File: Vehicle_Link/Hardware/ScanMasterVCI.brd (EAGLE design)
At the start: 53 x 39.4 mm, 97 parts, among them IC1 XMEGA32A4U, IC2 TL331, Q1 MMBT4403, Q10 ZXMP6A17G, Q2 MMBT3904, Q3 MMBT3904, Q4 MMBT4403, Q7 MMBT3904, Q8 MMBT4403, Q9 MMPQ3904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

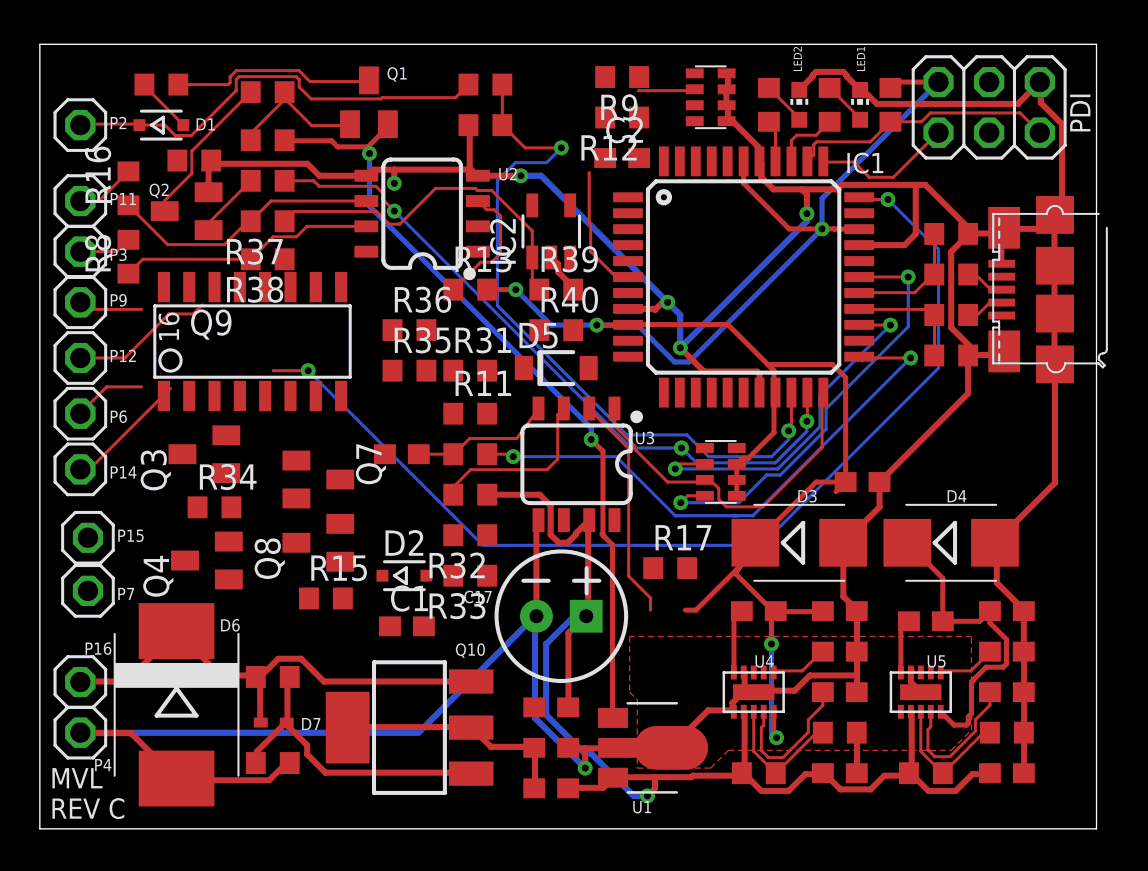
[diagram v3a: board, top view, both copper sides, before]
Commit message: CCD RX circuit tested. Don't have the firmware in a state to test the TX but I want to move forward with new boards for testing. I've finished re-laying out the board. Made a minor change to J1850, switched to a comparator for the RX.
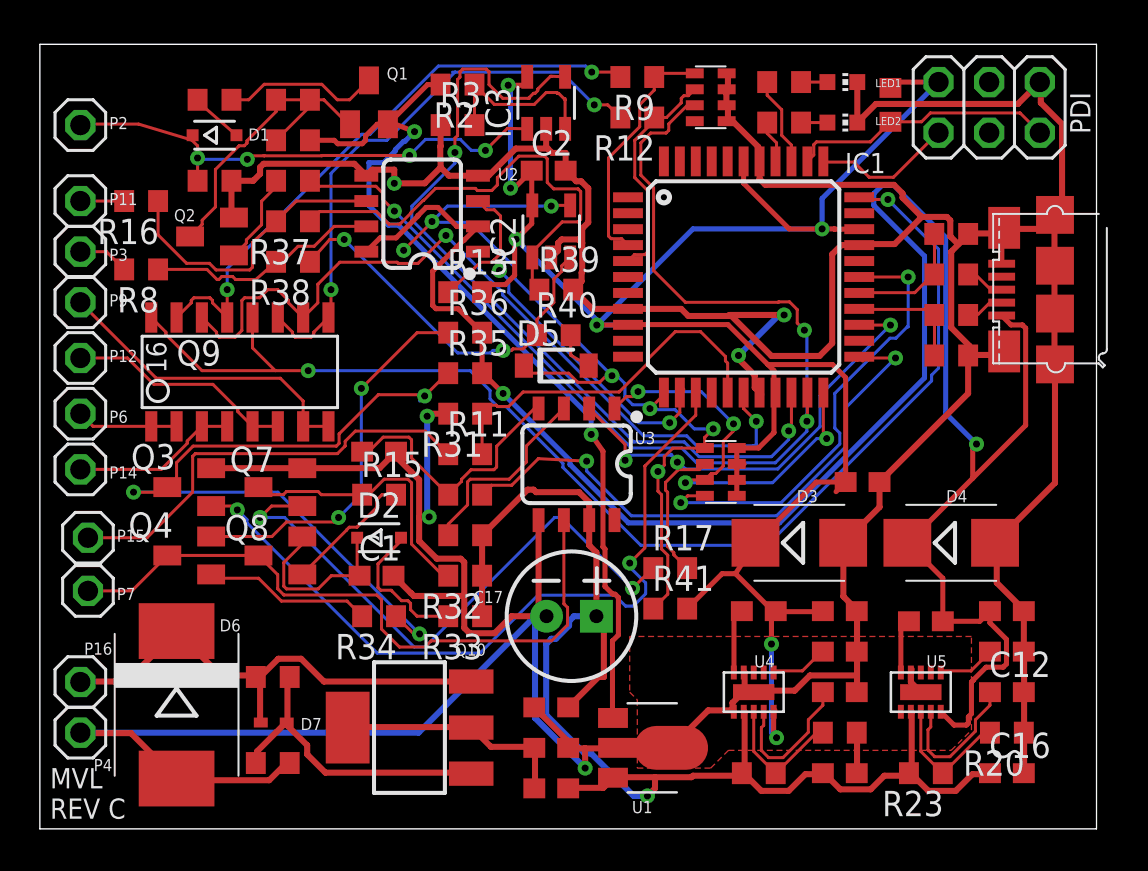
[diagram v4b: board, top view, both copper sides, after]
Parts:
- added IC3: TL331, linear:DBV-R-PDSO-G5
- added R41: 10k, adafruit:R0603
- R2: value 7.5k -> 1k
- R3: value 5k -> 1k
- moved R34 9.90 mm to (17.0, 10.7), turned to 180 degrees
- moved R15 5.85 mm to (17.0, 16.8)
- moved C2 3.74 mm to (25.5, 33.0)
- moved C1 2.96 mm to (16.9, 12.7)
- moved R35 2.80 mm to (21.3, 22.9)
- moved R36 2.80 mm to (21.3, 24.9)
- moved R1 2.77 mm to (8.76, 36.6)
- moved D1 2.71 mm to (8.76, 34.8)
- moved R24 2.56 mm to (37.3, 37.5), turned to 180 degrees
- moved LED2 2.33 mm to (40.3, 35.4), turned to 270 degrees
- moved D2 2.29 mm to (17.0, 14.6)
- moved R31 2.17 mm to (21.3, 20.8), turned to 180 degrees
- moved R10 2.05 mm to (21.3, 16.8)
- moved R11 2.05 mm to (21.3, 18.8)
- moved R14 2.05 mm to (21.3, 14.7)
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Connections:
- removed net SCI-A-ENGINE-EN: IC1.4
- removed net SCI-A-TRANS-EN: IC1.6
- removed net SCI-B-ENGINE-EN: IC1.5
- removed net SCI-B-TRANS-EN: IC1.7
- new net N$37: IC3.3, R2.1, R3.2
- net +3V3: now also IC3.5, R41.2
- net +8V: now also R2.2
- net CCD-RX: now also R41.1
- net GND: now also IC3.2
- net J1850VPW-RX: now also IC3.4; no longer R2.1, R3.2
- net J1962-2: now also IC3.1; no longer R2.2
- net SCI-A-EN: now also IC1.4
- net SCI-B-EN: now also IC1.5
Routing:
- net +5V: track 16.2 -> 104.2 mm, vias 0 -> 2
- net GND: track 237.3 -> 285.0 mm
- net CCD-RX: track 0.09 -> 46.7 mm, vias 0 -> 7
- net SCI-TRANS-TX: track 0.00 -> 40.5 mm, vias 0 -> 2
- net SCI-A-RX-EN: track 0.00 -> 38.4 mm, vias 0 -> 2
- net N$23: track 0.00 -> 38.3 mm, vias 0 -> 3
- net J1962-7: track 0.00 -> 33.8 mm
- net N$1: track 0.00 -> 30.1 mm, vias 0 -> 2
- net N$13: track 0.00 -> 29.4 mm, vias 0 -> 2
- net N$5: track 0.00 -> 28.5 mm, vias 0 -> 2
- net J1850VPW-TX: track 34.9 -> 57.8 mm
- net J1962-15: track 0.00 -> 22.0 mm
- net N$31: track 0.00 -> 19.3 mm, vias 0 -> 2
- net N$35: track 0.00 -> 19.2 mm, vias 0 -> 2
- net SCI-TRANS-RX: track 0.00 -> 18.5 mm
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
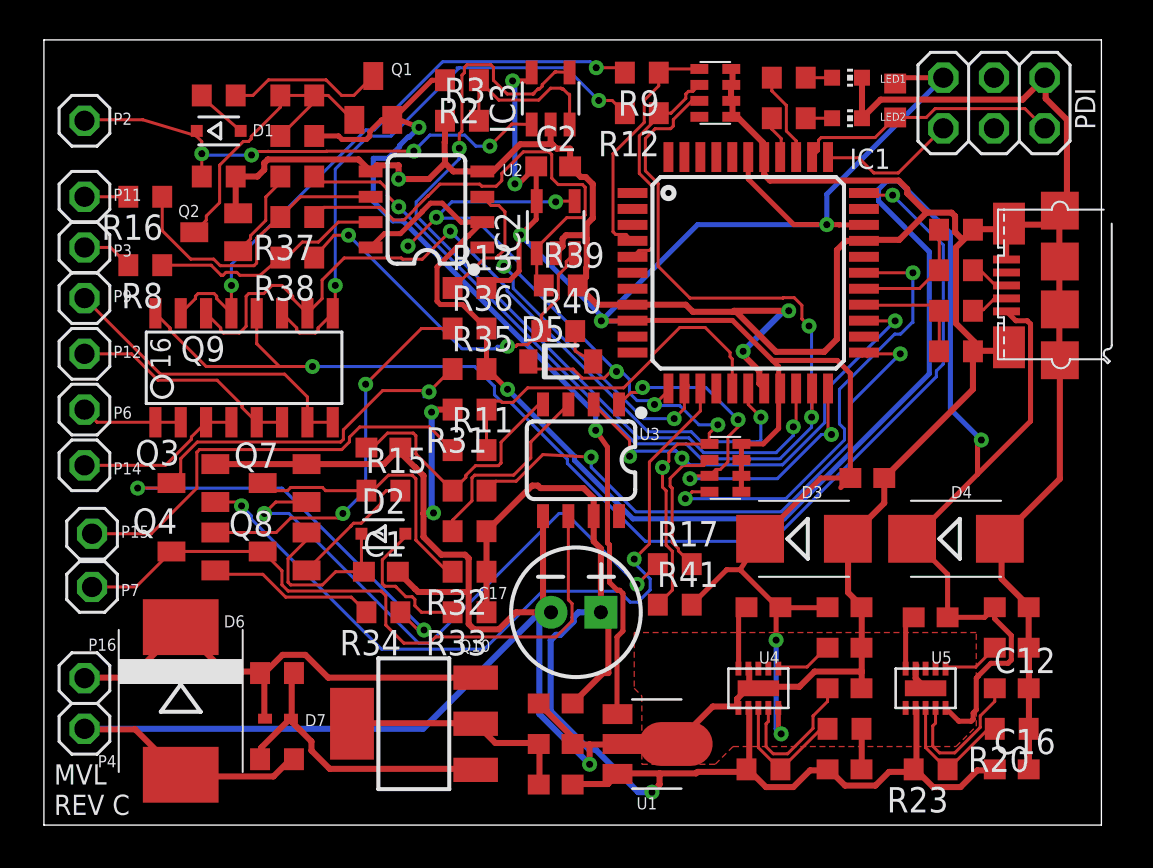
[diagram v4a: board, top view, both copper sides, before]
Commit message: Worked on the board layout some more - tried to trim down on some vias.
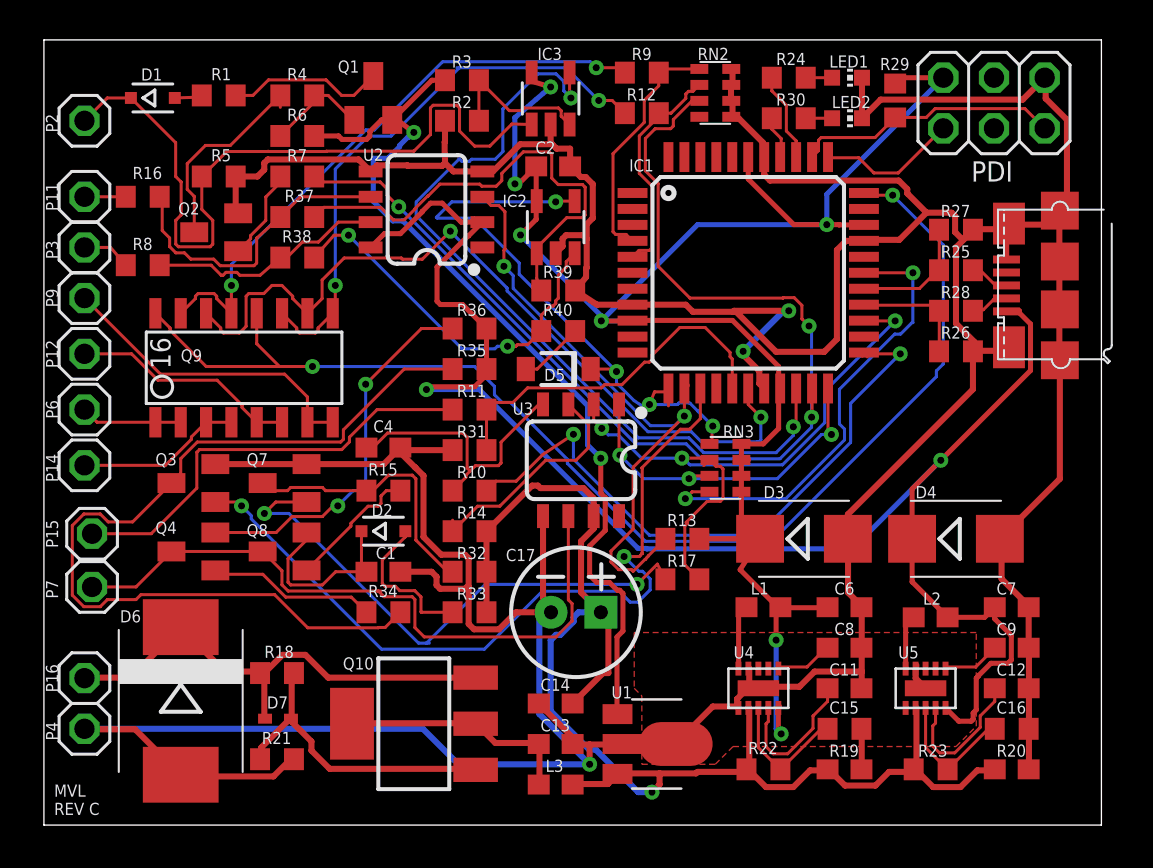
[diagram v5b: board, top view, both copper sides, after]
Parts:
- removed C3: 0.1uF, adafruit:C0603
- removed R41: 10k, adafruit:R0603
- moved R13 16.5 mm to (32.0, 14.4)
- moved D1 3.69 mm to (5.46, 36.4)
- moved R11 2.03 mm to (21.3, 20.8)
- moved R31 2.03 mm to (21.3, 18.8)
- moved R17 0.85 mm to (32.0, 12.3)
- moved D5 0.40 mm to (25.8, 22.9), turned to 180 degrees
- moved R39 0.28 mm to (25.8, 26.8)
- moved C1 0.13 mm to (17.0, 12.7)
- moved R16 0.13 mm to (4.95, 31.5)
- moved R8 0.13 mm to (4.95, 28.1)
- moved D2 0.13 mm to (17.0, 14.7)
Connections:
- net +3V3: no longer C3.1, R41.2
- net CCD-RX: no longer R41.1
- net GND: no longer C3.2
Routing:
- net +5V: track 104.2 -> 82.5 mm
- net +3V3: track 109.5 -> 93.3 mm
- net CCD-RX: track 46.7 -> 31.3 mm, vias 7 -> 4
- net J1962-2: track 25.8 -> 37.7 mm, vias 4 -> 0
- net CCD-TX: track 21.4 -> 31.8 mm
- net N$23: track 38.3 -> 45.2 mm, vias 3 -> 0
- net ISO-K-RX: track 22.5 -> 18.5 mm, vias 4 -> 3
- net GND: track 285.0 -> 281.2 mm, vias 6 -> 3
- net ISO-K-TX: track 30.2 -> 32.4 mm
- net N$13: track 29.4 -> 27.4 mm
- net ISO-K-EN: track 30.1 -> 32.1 mm
- net N$14: track 9.91 -> 11.7 mm
- net N$26: track 8.80 -> 10.3 mm
- net SCI-A-RX-EN: track 38.4 -> 39.7 mm
- net N$30: track 2.67 -> 1.43 mm
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
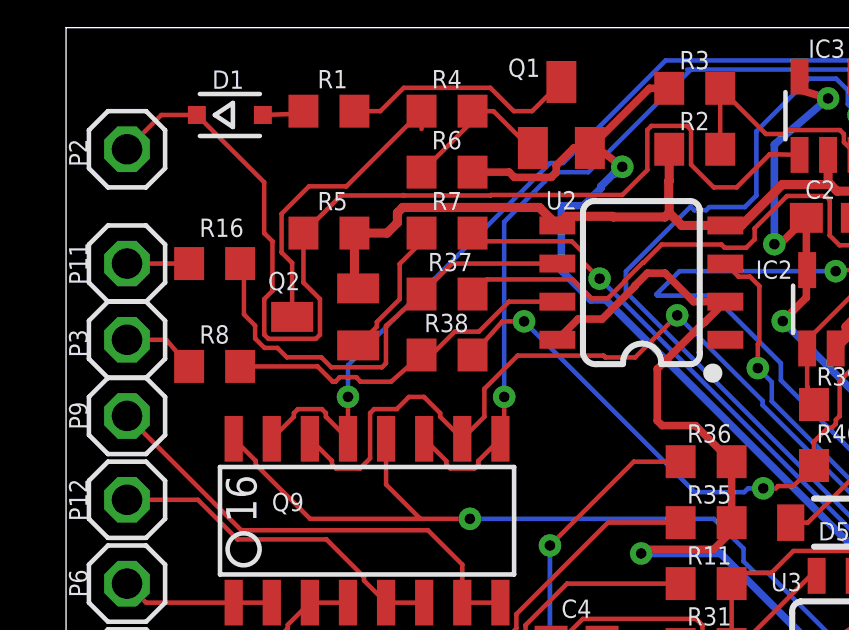
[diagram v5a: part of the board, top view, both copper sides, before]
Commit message: Reviewed the CCD circuit and found some small issues with the RX circuit, fixed.
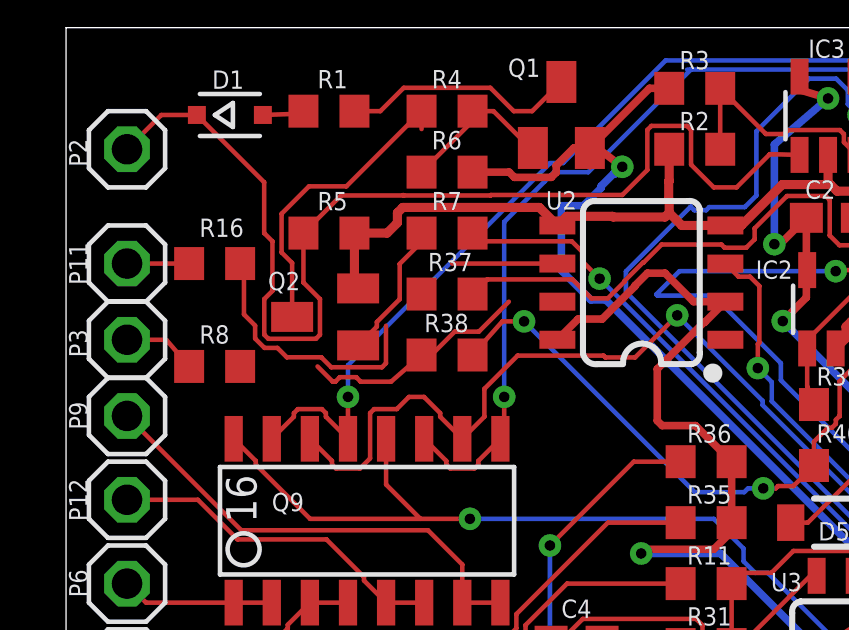
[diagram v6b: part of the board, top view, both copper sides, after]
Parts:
- R37: value 27.4k -> 40.2k
- R38: value 40.2k -> 27.4k
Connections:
- removed net N$32: R16.1, R37.2, U2.6
- new net N$39: R37.2, R8.1, U2.7
- net N$33: now also R16.1, U2.6; no longer R8.1, U2.7
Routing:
- net N$32: track 15.3 -> 0.00 mm
- net N$33: track 12.0 -> 20.1 mm
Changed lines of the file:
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@@
 <?xml version="1.0" encoding="utf-8"?>
 <!DOCTYPE eagle SYSTEM "eagle.dtd">
-<eagle version="8.7.0">
+<eagle version="8.4.3">
 <drawing>
 <settings>
@@
 <param name="checkRestrict" value="1"/>
 <param name="checkStop" value="0"/>
-<param name="checkValues" value="0"/>
 <param name="useDiameter" value="13"/>
 <param name="maxErrors" value="50"/>
@@
 <attribute name="NAME" x="4.445" y="32.385" size="0.6096" layer="25"/>
 </element>
-<element name="R37" library="adafruit" library_urn="urn:adsk.eagle:library:420" package="R0603" value="27.4k" x="12.7" y="30.48" smashed="yes" rot="R180">
+<element name="R37" library="adafruit" library_urn="urn:adsk.eagle:library:420" package="R0603" value="40.2k" x="12.7" y="30.48" smashed="yes" rot="R180">
 <attribute name="NAME" x="12.065" y="31.242" size="0.6096" layer="25"/>
 </element>
-<element name="R38" library="adafruit" library_urn="urn:adsk.eagle:library:420" package="R0603" value="40.2k" x="12.7" y="28.448" smashed="yes" rot="R180">
+<element name="R38" library="adafruit" library_urn="urn:adsk.eagle:library:420" package="R0603" value="27.4k" x="12.7" y="28.448" smashed="yes" rot="R180">
 <attribute name="NAME" x="11.938" y="29.21" size="0.6096" layer="25"/>
 </element>
@@
 <wire x1="15.494" y1="16.764" x2="16.129" y2="16.764" width="0.1524" layer="16"/>
 </signal>
-<signal name="N$32">
+<signal name="N$33">
+<contactref element="R38" pad="2"/>
+<wire x1="8.382" y1="28.067" x2="8.89" y2="27.559" width="0.1524" layer="1"/>
+<wire x1="10.834" y1="27.559" x2="11.85" y2="28.448" width="0.1524" layer="1"/>
+<wire x1="8.89" y1="27.559" x2="8.9760125" y2="27.559" width="0.1524" layer="1"/>
+<wire x1="8.9760125" y1="27.559" x2="9.1256125" y2="27.7086" width="0.1524" layer="1"/>
+<wire x1="9.1256125" y1="27.7086" x2="9.6703875" y2="27.7086" width="0.1524" layer="1"/>
+<wire x1="9.6703875" y1="27.7086" x2="9.8199875" y2="27.559" width="0.1524" layer="1"/>
+<wire x1="9.8199875" y1="27.559" x2="10.834" y2="27.559" width="0.1524" layer="1"/>
+<wire x1="12.1767125" y1="28.448" x2="11.85" y2="28.448" width="0.1524" layer="1"/>
+<wire x1="12.9553125" y1="29.2266" x2="12.1767125" y2="28.448" width="0.1524" layer="1"/>
+<wire x1="13.760615625" y1="29.2266" x2="12.9553125" y2="29.2266" width="0.1524" layer="1"/>
+<wire x1="14.760015625" y1="30.226" x2="13.760615625" y2="29.2266" width="0.1524" layer="1"/>
 <contactref element="R16" pad="1"/>
 <contactref element="U2" pad="6"/>
-<contactref element="R37" pad="2"/>
 <wire x1="10.6646" y1="28.1733125" x2="10.5306875" y2="28.0394" width="0.1524" layer="1"/>
-<wire x1="11.85" y1="30.48" x2="10.6646" y2="29.4216" width="0.1524" layer="1"/>
 <wire x1="10.6646" y1="29.4216" x2="10.6646" y2="28.1733125" width="0.1524" layer="1"/>
 <wire x1="8.84065625" y1="28.0394" x2="8.50825625" y2="28.3718" width="0.1524" layer="1"/>
 <wire x1="8.50825625" y1="28.3718" x2="7.3589125" y2="28.3718" width="0.1524" layer="1"/>
 <wire x1="10.5306875" y1="28.0394" x2="8.84065625" y2="28.0394" width="0.1524" layer="1"/>
-<wire x1="11.85" y1="30.48" x2="12.866" y2="31.496" width="0.1524" layer="1"/>
 <wire x1="12.866" y1="31.496" x2="16.377" y2="31.496" width="0.1524" layer="1"/>
 <wire x1="7.3589125" y1="28.3718" x2="7.0461125" y2="28.6846" width="0.1524" layer="1"/>
@@
 <wire x1="5.93" y1="29.8007125" x2="5.93" y2="31.369" width="0.1524" layer="1"/>
 <wire x1="5.93" y1="31.369" x2="5.803" y2="31.496" width="0.1524" layer="1"/>
-</signal>
-<signal name="N$33">
-<contactref element="R8" pad="1"/>
-<contactref element="U2" pad="7"/>
-<contactref element="R38" pad="2"/>
-<wire x1="8.382" y1="28.067" x2="8.89" y2="27.559" width="0.1524" layer="1"/>
-<wire x1="10.834" y1="27.559" x2="11.85" y2="28.448" width="0.1524" layer="1"/>
-<wire x1="8.89" y1="27.559" x2="8.9760125" y2="27.559" width="0.1524" layer="1"/>
-<wire x1="8.9760125" y1="27.559" x2="9.1256125" y2="27.7086" width="0.1524" layer="1"/>
-<wire x1="9.1256125" y1="27.7086" x2="9.6703875" y2="27.7086" width="0.1524" layer="1"/>
-<wire x1="9.6703875" y1="27.7086" x2="9.8199875" y2="27.559" width="0.1524" layer="1"/>
-<wire x1="9.8199875" y1="27.559" x2="10.834" y2="27.559" width="0.1524" layer="1"/>
-<wire x1="5.803" y1="28.067" x2="8.382" y2="28.067" width="0.1524" layer="1"/>
-<wire x1="12.1767125" y1="28.448" x2="11.85" y2="28.448" width="0.1524" layer="1"/>
-<wire x1="12.9553125" y1="29.2266" x2="12.1767125" y2="28.448" width="0.1524" layer="1"/>
-<wire x1="13.760615625" y1="29.2266" x2="12.9553125" y2="29.2266" width="0.1524" layer="1"/>
-<wire x1="16.377" y1="30.226" x2="14.760015625" y2="30.226" width="0.1524" layer="1"/>
-<wire x1="14.760015625" y1="30.226" x2="13.760615625" y2="29.2266" width="0.1524" layer="1"/>
+<wire x1="14.760015625" y1="30.226" x2="16.377" y2="31.496" width="0" layer="19" extent="1-1"/>
+<wire x1="8.50825625" y1="28.3718" x2="8.382" y2="28.067" width="0" layer="19" extent="1-1"/>
 </signal>
 <signal name="N$34">
@@
 <wire x1="24.0553125" y1="35.9462" x2="25.7946875" y2="35.9462" width="0.1524" layer="1"/>
 </signal>
+<signal name="N$39">
+<contactref element="R8" pad="1"/>
+<contactref element="U2" pad="7"/>
+<contactref element="R37" pad="2"/>
+<wire x1="11.85" y1="30.48" x2="16.377" y2="30.226" width="0" layer="19" extent="1-1"/>
+<wire x1="5.803" y1="28.067" x2="11.85" y2="30.48" width="0" layer="19" extent="1-1"/>
+</signal>
 </signals>
